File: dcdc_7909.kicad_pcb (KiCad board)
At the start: 4 copper layers, 41.5 x 27 mm, 60 parts, among them J1 V_IN, J2 G_IN, J3 RFShield_Clip, J4 RFShield_Clip, J5 RFShield_Clip, J6 RFShield_Clip, J7 +10V, J8 G_OUT, J9 -10V, U1 LM2940-SOT223-15, U2 LT3471, U3 LT3045xMSE, U4 LT3094xMSE

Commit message: Rev 2.1 finished.
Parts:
- C12: value 470p -> 150p
- C17, C18: value 10u -> 22u; footprint Capacitor_SMD:C_0805_2012Metric -> Capacitor_SMD:C_1206_3216Metric
- C6: value 2200p -> 150p
- R2, R4: value DNP -> 2k
- R3: value 18k -> 20k
- R5: value 2k -> DNP
- R6: value 20k -> 22k
- moved C18 1.46 mm to (85.1, 67.4), turned to 90 degrees
- moved R7 0.58 mm to (87.5, 57.7)
- moved C17 0.56 mm to (87.9, 55.8)
- moved C16 0.53 mm to (81.1, 64.2)
- moved U4 0.53 mm to (85.0, 61.6)
- moved C22 0.53 mm to (89.0, 62.6)
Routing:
- net Net-(C17-Pad1): track 4.46 -> 3.76 mm
- net GND: vias 131 -> 138
- added copper zone on In2.Cu, net /-10.5V

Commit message: Final v2.1.
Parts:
- R2, R4: value 2k -> 2k05

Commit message: V2.1 ready for JLCPCB.
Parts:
- moved R9 1.37 mm to (93.1, 67.4)
- moved R10 0.86 mm to (92.7, 75.5)
- moved R1 0.77 mm to (109.7, 72.2)
- moved C4 0.74 mm to (109.7, 74.7)
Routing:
- net /+10V: track 13.1 -> 14.8 mm
- net Net-(D4-Pad2): track 3.17 -> 4.51 mm
- net Net-(C4-Pad1): track 28.8 -> 27.8 mm
- net Net-(D5-Pad1): track 3.88 -> 4.81 mm
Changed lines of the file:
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@@
   )
   (footprint "Resistor_SMD:R_0603_1608Metric" (layer "F.Cu")
-    (at 92.329 74.676 90)
+    (at 92.71 75.4502 90)
     (descr "Resistor SMD 0603 (1608 Metric), square (rectangular) end terminal, IPC_7351 nominal, (Body size source: IPC-SM-782 page 72, https://www.pcb-3d.com/wordpress/wp-content/uploads/ipc-sm-782a_amendment_1_and_2.pdf), generated with kicad-footprint-generator")
     (tags "resistor")
@@
   )
   (footprint "Resistor_SMD:R_0603_1608Metric" (layer "F.Cu")
-    (at 92.202 68.389 -90)
+    (at 93.1164 67.373 -90)
     (descr "Resistor SMD 0603 (1608 Metric), square (rectangular) end terminal, IPC_7351 nominal, (Body size source: IPC-SM-782 page 72, https://www.pcb-3d.com/wordpress/wp-content/uploads/ipc-sm-782a_amendment_1_and_2.pdf), generated with kicad-footprint-generator")
     (tags "resistor")
@@
     (property "Sheetname" "")
     (attr smd)
-    (fp_text reference "R9" (at -2.222 0 90) (layer "F.SilkS")
+    (fp_text reference "R9" (at -0.063 1.1176 90) (layer "F.SilkS")
       (effects (font (size 1 1) (thickness 0.15)))
     )
@@
     (property "Sheetname" "")
     (attr smd)
-    (fp_text reference "C11" (at 2.7414 0 90) (layer "F.SilkS")
+    (fp_text reference "C11" (at 0.6858 2.0574 180) (layer "F.SilkS")
       (effects (font (size 1 1) (thickness 0.15)))
     )
@@
   )
   (footprint "Capacitor_SMD:C_0603_1608Metric" (layer "F.Cu")
-    (at 110.3884 75.0316 -90)
+    (at 109.728 74.689 -90)
     (descr "Capacitor SMD 0603 (1608 Metric), square (rectangular) end terminal, IPC_7351 nominal, (Body size source: IPC-SM-782 page 76, https://www.pcb-3d.com/wordpress/wp-content/uploads/ipc-sm-782a_amendment_1_and_2.pdf), generated with kicad-footprint-generator")
     (tags "capacitor")
@@
     (property "Sheetname" "")
     (attr smd)
-    (fp_text reference "C4" (at -4.2164 -0.2032 90) (layer "F.SilkS")
+    (fp_text reference "C4" (at 1.8666 0 180) (layer "F.SilkS")
       (effects (font (size 1 1) (thickness 0.15)))
     )
@@
   )
   (footprint "Resistor_SMD:R_0402_1005Metric" (layer "F.Cu")
-    (at 110.3884 72.4916 -90)
+    (at 109.6772 72.1888 -90)
     (descr "Resistor SMD 0402 (1005 Metric), square (rectangular) end terminal, IPC_7351 nominal, (Body size source: IPC-SM-782 page 72, https://www.pcb-3d.com/wordpress/wp-content/uploads/ipc-sm-782a_amendment_1_and_2.pdf), generated with kicad-footprint-generator")
     (tags "resistor")
@@
     (property "Sheetname" "")
     (attr smd)
-    (fp_text reference "R1" (at 4.6482 0 90) (layer "F.SilkS")
+    (fp_text reference "R1" (at 0.0488 -0.9652 90) (layer "F.SilkS")
       (effects (font (size 1 1) (thickness 0.15)))
     )
@@
   )
   (segment (start 101.854 73.1266) (end 101.854 73.41865) (width 1.016) (layer "F.Cu") (net 1))
+  (segment (start 110.4392 71.6788) (end 111.76 70.358) (width 0.25) (layer "F.Cu") (net 1))
   (segment (start 98.171 63.43645) (end 97.24395 62.5094) (width 0.762) (layer "F.Cu") (net 1))
   (segment (start 112.635 73.304) (end 112.635 71.233) (width 0.762) (layer "F.Cu") (net 1))
-  (segment (start 110.3884 71.9816) (end 110.3884 71.7296) (width 0.254) (layer "F.Cu") (net 1))
   (segment (start 104.8004 72.7474) (end 105.078 73.025) (width 1.016) (layer "F.Cu") (net 1))
   (segment (start 98.171 65.786) (end 98.171 63.43645) (width 0.762) (layer "F.Cu") (net 1))
   (segment (start 104.8004 70.5866) (end 104.8004 72.7474) (width 1.016) (layer "F.Cu") (net 1))
-  (segment (start 110.3884 71.7296) (end 111.76 70.358) (width 0.254) (layer "F.Cu") (net 1))
   (segment (start 105.078 73.025) (end 102.24765 73.025) (width 1.016) (layer "F.Cu") (net 1))
   (segment (start 98.9838 66.5988) (end 98.171 65.786) (width 0.762) (layer "F.Cu") (net 1))
   (segment (start 112.635 71.233) (end 111.76 70.358) (width 0.762) (layer "F.Cu") (net 1))
+  (segment (start 109.6772 71.6788) (end 110.4392 71.6788) (width 0.25) (layer "F.Cu") (net 1))
   (segment (start 101.8772 66.6496) (end 99.568 66.6496) (width 0.254) (layer "F.Cu") (net 1))
   (segment (start 99.5172 66.5988) (end 98.9838 66.5988) (width 0.762) (layer "F.Cu") (net 1))
@@
   (segment (start 101.8772 67.1496) (end 100.9984 67.1496) (width 0.1524) (layer "F.Cu") (net 4))
   (segment (start 100.9476 66.1496) (end 100.8211 66.0231) (width 0.1524) (layer "F.Cu") (net 4))
-  (segment (start 110.3884 73.0016) (end 109.5228 73.0016) (width 0.1524) (layer "F.Cu") (net 4))
+  (segment (start 109.6772 72.6988) (end 110.227 72.6988) (width 0.25) (layer "F.Cu") (net 4))
+  (segment (start 109.728 72.7496) (end 109.6772 72.6988) (width 0.25) (layer "F.Cu") (net 4))
   (segment (start 101.8772 66.1496) (end 100.9476 66.1496) (width 0.1524) (layer "F.Cu") (net 4))
-  (segment (start 109.5228 73.0016) (end 109.474 73.0504) (width 0.1524) (layer "F.Cu") (net 4))
+  (segment (start 109.728 73.914) (end 109.728 72.7496) (width 0.25) (layer "F.Cu") (net 4))
   (segment (start 100.9984 67.1496) (end 100.838 67.31) (width 0.1524) (layer "F.Cu") (net 4))
   (segment (start 100.8211 66.0231) (end 100.838 66.0231) (width 0.1524) (layer "F.Cu") (net 4))
-  (segment (start 110.3884 74.2566) (end 110.3884 73.0016) (width 0.1524) (layer "F.Cu") (net 4))
+  (segment (start 110.227 72.6988) (end 110.5916 73.0634) (width 0.25) (layer "F.Cu") (net 4))
   (via (at 100.838 67.31) (size 0.6) (drill 0.3) (layers "F.Cu" "B.Cu") (free) (net 4))
   (via (at 100.838 66.0231) (size 0.6) (drill 0.3) (layers "F.Cu" "B.Cu") (net 4))
-  (via (at 109.474 73.0504) (size 0.6) (drill 0.3) (layers "F.Cu" "B.Cu") (net 4))
-  (segment (start 113.3348 72.136) (end 112.4204 73.0504) (width 0.1524) (layer "In2.Cu") (net 4))
+  (via (at 110.5916 73.0634) (size 0.6) (drill 0.3) (layers "F.Cu" "B.Cu") (net 4))
   (segment (start 100.838 67.31) (end 100.838 66.0231) (width 0.1524) (layer "In2.Cu") (net 4))
   (segment (start 110.6932 64.77) (end 113.3348 67.4116) (width 0.1524) (layer "In2.Cu") (net 4))
+  (segment (start 112.4074 73.0634) (end 110.5916 73.0634) (width 0.1524) (layer "In2.Cu") (net 4))
   (segment (start 113.3348 67.4116) (end 113.3348 72.136) (width 0.1524) (layer "In2.Cu") (net 4))
+  (segment (start 113.3348 72.136) (end 112.4074 73.0634) (width 0.1524) (layer "In2.Cu") (net 4))
   (segment (start 100.838 66.0231) (end 102.0911 64.77) (width 0.1524) (layer "In2.Cu") (net 4))
-  (segment (start 112.4204 73.0504) (end 109.474 73.0504) (width 0.1524) (layer "In2.Cu") (net 4))
   (segment (start 102.0911 64.77) (end 110.6932 64.77) (width 0.1524) (layer "In2.Cu") (net 4))
   (segment (start 107.3216 69.4824) (end 107.2896 69.5144) (width 0.254) (layer "F.Cu") (net 7))
@@
   (segment (start 104.9108 67.7832) (end 107.2896 67.7832) (width 0.1524) (layer "F.Cu") (net 10))
   (segment (start 89.027 66.837) (end 89.2 67.01) (width 0.508) (layer "F.Cu") (net 11))
-  (segment (start 92.202 67.564) (end 89.754 67.564) (width 0.3048) (layer "F.Cu") (net 11))
+  (segment (start 92.6544 67.01) (end 89.2 67.01) (width 0.25) (layer "F.Cu") (net 11))
   (segment (start 89.027 64.0552) (end 89.027 66.837) (width 0.508) (layer "F.Cu") (net 11))
+  (segment (start 93.1164 66.548) (end 92.6544 67.01) (width 0.25) (layer "F.Cu") (net 11))
   (via (at 81.9912 68.1228) (size 0.8) (drill 0.4) (layers "F.Cu" "B.Cu") (net 11))
   (segment (start 89.2 67.01) (end 83.104 67.01) (width 1.016) (layer "B.Cu") (net 11))
@@
   (segment (start 81.8642 55.753) (end 83.009 55.753) (width 1.016) (layer "F.Cu") (net 12))
   (segment (start 83.009 55.753) (end 83.136 55.626) (width 1.016) (layer "F.Cu") (net 12))
-  (segment (start 92.329 75.501) (end 90.709 75.501) (width 0.3048) (layer "F.Cu") (net 12))
   (segment (start 86.819 79.248) (end 86.962 79.248) (width 0.762) (layer "F.Cu") (net 12))
   (segment (start 86.962 79.248) (end 89.2 77.01) (width 0.762) (layer "F.Cu") (net 12))
-  (segment (start 90.709 75.501) (end 89.2 77.01) (width 0.3048) (layer "F.Cu") (net 12))
+  (segment (start 91.9752 77.01) (end 89.2 77.01) (width 0.25) (layer "F.Cu") (net 12))
+  (segment (start 92.71 76.2752) (end 91.9752 77.01) (width 0.25) (layer "F.Cu") (net 12))
   (via (at 81.8642 55.753) (size 0.8) (drill 0.4) (layers "F.Cu" "B.Cu") (net 12))
   (segment (start 82.6996 77.01) (end 80.6196 74.93) (width 1.016) (layer "In2.Cu") (net 12))
@@
   (segment (start 80.6196 74.93) (end 80.6196 63.5508) (width 1.016) (layer "In2.Cu") (net 12))
   (segment (start 81.1784 56.4388) (end 81.8642 55.753) (width 1.016) (layer "In2.Cu") (net 12))
-  (segment (start 92.202 69.214) (end 91.9744 69.214) (width 0.254) (layer "F.Cu") (net 13))
-  (segment (start 91.9744 69.214) (end 91.2876 69.9008) (width 0.254) (layer "F.Cu") (net 13))
+  (segment (start 93.1164 68.198) (end 92.9904 68.198) (width 0.25) (layer "F.Cu") (net 13))
+  (segment (start 92.9904 68.198) (end 91.2876 69.9008) (width 0.25) (layer "F.Cu") (net 13))
   (via (at 91.2876 69.9008) (size 0.6) (drill 0.3) (layers "F.Cu" "B.Cu") (net 13))
   (segment (start 92.819 68.834) (end 92.3544 68.834) (width 0.254) (layer "B.Cu") (net 13))
   (segment (start 92.3544 68.834) (end 91.2876 69.9008) (width 0.254) (layer "B.Cu") (net 13))
-  (segment (start 91.5924 73.1144) (end 92.329 73.851) (width 0.254) (layer "F.Cu") (net 14))
-  (segment (start 91.5924 72.009) (end 91.5924 73.1144) (width 0.254) (layer "F.Cu") (net 14))
+  (segment (start 91.5924 73.5076) (end 92.71 74.6252) (width 0.25) (layer "F.Cu") (net 14))
+  (segment (start 91.5924 72.009) (end 91.5924 73.5076) (width 0.25) (layer "F.Cu") (net 14))
   (via (at 91.5924 72.009) (size 0.6) (drill 0.3) (layers "F.Cu" "B.Cu") (net 14))
   (segment (start 91.5924 71.9656) (end 92.819 70.739) (width 0.254) (layer "B.Cu") (net 14))

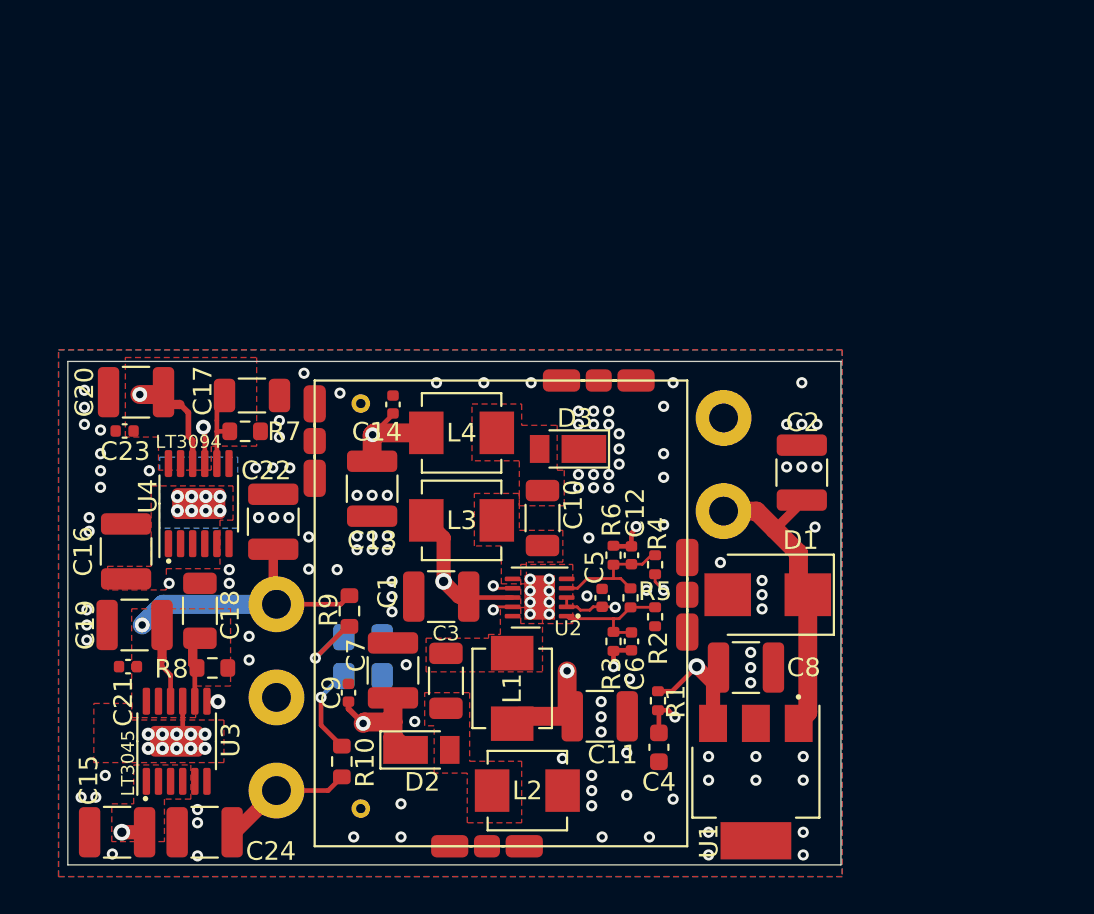
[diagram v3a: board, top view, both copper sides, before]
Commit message: Reworking the board with MAX76x/
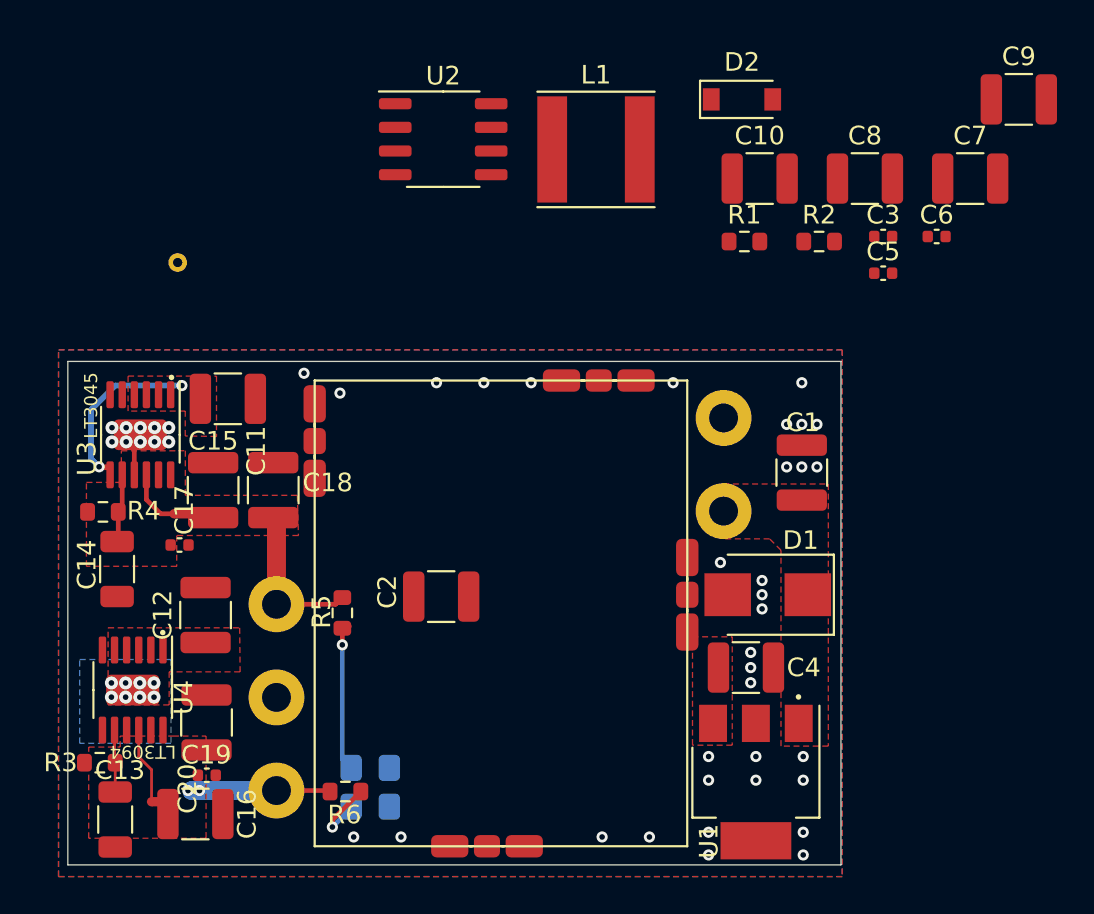
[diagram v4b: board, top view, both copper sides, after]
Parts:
- removed the C11 at (106.6, 73.0)
- removed the C12 at (108.3, 64.4)
- removed the C13 at (94.3, 60.8)
- removed the C14 at (95.5, 56.3)
- removed the C4 at (109.7, 74.7)
- removed the D3 at (104.9, 58.7)
- removed L2, L3, L4: 10u, Inductor_SMD:L_Vishay_IHLP-1616
- removed the R3 at (107.3, 69.0)
- removed the R4 at (109.5, 64.9)
- removed the R5 at (108.2, 66.7)
- removed the R6 at (107.3, 64.4)
- removed the TP1 at (93.7, 78.0)
- added C8: 22u, Capacitor_SMD:C_1210_3225Metric, F.Cu at (120.8, 44.2)
- C10: value 4u7 -> 22u; footprint Capacitor_SMD:C_1206_3216Metric -> Capacitor_SMD:C_1210_3225Metric
- C3: value 4u7 -> 100n; footprint Capacitor_SMD:C_1206_3216Metric -> Capacitor_SMD:C_0402_1005Metric
- C6: value 150p -> 100n
- C9: value 10n -> 22u; footprint Capacitor_SMD:C_0402_1005Metric -> Capacitor_SMD:C_1210_3225Metric
- D2: value D_Schottky -> 1N5817; footprint Diode_SMD:D_PowerDI-123 -> Diode_SMD:D_SOD-123
- L1: value 10u -> 47u; footprint Inductor_SMD:L_Vishay_IHLP-1616 -> Inductor_SMD:L_Taiyo-Yuden_NR-60xx
- R1: value 20k -> 1M07 1%; footprint Resistor_SMD:R_0402_1005Metric -> Resistor_SMD:R_0603_1608Metric
- R2: value 2k05 -> 150k 1%; footprint Resistor_SMD:R_0402_1005Metric -> Resistor_SMD:R_0603_1608Metric
- TP1: renamed from TP2; value -10.5V -> -10.7
- U2: value LT3471 -> MAX764; footprint Package_DFN_QFN:DFN-10-1EP_3x3mm_P0.5mm_EP1.65x2.38mm -> Package_SO:SO-8_3.9x4.9mm_P1.27mm
- moved C9 48.1 mm to (129.0, 39.9), turned to 0 degrees
- moved C7 40.7 mm to (126.4, 44.2), turned to 0 degrees
- moved D2 38.9 mm to (114.2, 39.9)
- moved C3 33.5 mm to (121.8, 47.3), turned to 0 degrees
- moved L1 29.3 mm to (106.3, 42.6), turned to 0 degrees
- moved C6 27.2 mm to (124.6, 47.3), turned to 0 degrees
- moved U2 25.1 mm to (98.1, 42.0), turned to 0 degrees
- moved R1 25.1 mm to (114.3, 47.5), turned to 0 degrees
- moved C11 24.0 mm to (86.6, 56.0), turned to 0 degrees
- moved C13 23.9 mm to (80.5, 78.6), turned to -90 degrees
- moved C5 23.1 mm to (121.8, 49.2), turned to 0 degrees
- moved C16 22.9 mm to (84.8, 78.3), turned to 0 degrees
- moved R2 22.0 mm to (118.3, 47.5), turned to 0 degrees
- moved C10 21.6 mm to (115.1, 44.2), turned to 0 degrees
- moved NT2 21.3 mm to (83.0, 77.6), turned to 0 degrees
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- renumbered C2 to C1, C15 to C11, C16 to C12, C17 to C13, C18 to C14, C19 to C15, C20 to C16, C21 to C17, C22 to C18, C23 to C19, C1 to C2, C24 to C20, C8 to C4, D4 to D3, D5 to D4, R7 to R3, R8 to R4, R9 to R5, R10 to R6
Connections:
- C10 pad 1: Net-(C10-Pad1) -> VCC
- C10 pad 2: Net-(C10-Pad2) -> GND
- C11 pad 1: /+10.5V -> VCC
- C12 pad 1: /-10.5V -> /-10.7
- C3 pad 1: Net-(C3-Pad1) -> VCC
- C3 pad 2: Net-(C3-Pad2) -> GND
- C6 pad 1: /+10.5V -> /-10.7
- C6 pad 2: Net-(C6-Pad2) -> GND
- C7 pad 1: /+10.5V -> /-10.7
- C9 pad 1: /+10.5V -> /-10.7
- D2 pad 1: /+10.5V -> Net-(D2-Pad1)
- D2 pad 2: Net-(C3-Pad2) -> /-10.7
- L1 pad 1: VCC -> Net-(D2-Pad1)
- L1 pad 2: Net-(C3-Pad1) -> GND
- R1 pad 1: VCC -> Net-(R1-Pad1)
- R1 pad 2: Net-(C4-Pad1) -> /-10.7
- R2 pad 1: GND -> Net-(C5-Pad1)
- R2 pad 2: Net-(C6-Pad2) -> Net-(R1-Pad1)
- TP1 pad 1: /-10.5V -> /-10.7
- U2 pad 1: Net-(C6-Pad2) -> /-10.7
- U2 pad 2: Net-(C5-Pad1) -> Net-(R1-Pad1)
- U2 pad 3: Net-(C5-Pad1) -> GND
- U2 pad 4: Net-(C12-Pad2) -> Net-(C5-Pad1)
- U2 pad 6: Net-(C10-Pad1) -> VCC
- U2 pad 7: Net-(C4-Pad1) -> VCC
- U2 pad 8: VCC -> Net-(D2-Pad1)
- U3 pad 1: /+10.5V -> VCC
- U3 pad 2: /+10.5V -> VCC
- U3 pad 3: /+10.5V -> VCC
- U3 pad 4: /+10.5V -> VCC
- U3 pad 7: /+10.5V -> VCC
- U4 pad 1: /-10.5V -> /-10.7
- U4 pad 13: /-10.5V -> /-10.7
- U4 pad 2: /-10.5V -> /-10.7
- U4 pad 3: /-10.5V -> /-10.7
- U4 pad 5: /-10.5V -> /-10.7
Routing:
- net /+10.5V: track 62.9 -> 0.00 mm, vias 4 -> 0
- net /-10.5V: track 40.7 -> 0.00 mm, vias 10 -> 0
- net /-10V: track 37.6 -> 7.32 mm, vias 1 -> 2
- net VCC: track 38.2 -> 9.37 mm, vias 3 -> 2
- net Net-(C4-Pad1): track 27.8 -> 0.00 mm, vias 3 -> 0
- net Net-(C1-Pad1): track 16.0 -> 0.00 mm
- net Net-(C5-Pad1): track 7.60 -> 0.00 mm, vias 2 -> 0
- net Net-(C12-Pad2): track 6.85 -> 0.00 mm
- net Net-(C6-Pad2): track 6.54 -> 0.00 mm
- net /+10V: track 14.8 -> 8.41 mm, vias 1 -> 0
- net Net-(D3-Pad2): track 4.51 -> 7.82 mm
- net GND: track 3.76 -> 2.28 mm, vias 138 -> 44
- net Net-(NT2-Pad1): track 2.92 -> 4.13 mm
- net Net-(D4-Pad1): track 4.81 -> 4.05 mm
- net Net-(NT1-Pad1): track 2.46 -> 3.13 mm
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- added copper zone on B.Cu, net /-10.7
- added copper zone on F.Cu, net /-10.7
- added copper zone on F.Cu, net Net-(C1-Pad1)
- added copper zone on F.Cu, net VCC
- removed copper zone on F.Cu, net /+10.5V
- removed copper zone on B.Cu, net /-10.5V
- removed copper zone on F.Cu, net /-10.5V
- removed copper zone on In2.Cu, net /-10.5V
- removed copper zone on F.Cu, net Net-(C10-Pad1)
- removed copper zone on F.Cu, net Net-(C10-Pad2)
- removed copper zone on F.Cu, net Net-(C3-Pad1)
- removed copper zone on F.Cu, net Net-(C3-Pad2)
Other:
- board text removed: "+"
- board text removed: "+10V"
- board text removed: "-10V"

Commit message: Reworking almost completed.
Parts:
- added C1: 22u, Capacitor_SMD:C_1210_3225Metric, F.Cu at (108.8, 71.2)
- D2: footprint Diode_SMD:D_SOD-123 -> Diode_SMD:D_PowerDI-123
- J3, J4, J5, J6: value RFShield_Clip -> Conn_01x01; footprint marcin_library:S0971-46R -> Connector_Wire:SolderWirePad_1x01_SMD_1x2mm
- R1, R2, R5, R6: footprint Resistor_SMD:R_0603_1608Metric -> Resistor_SMD:R_0402_1005Metric
- moved C10 44.7 mm to (93.7, 67.3), turned to 90 degrees
- moved C9 38.9 mm to (93.7, 72.0), turned to -90 degrees
- moved C7 37.7 mm to (96.8, 72.8), turned to -90 degrees
- moved C8 36.4 mm to (98.0, 66.9)
- moved C6 36.3 mm to (98.1, 76.8), turned to -90 degrees
- moved D2 34.1 mm to (97.9, 69.8), turned to 180 degrees
- moved R2 33.4 mm to (98.1, 74.2), turned to 90 degrees
- moved R1 32.2 mm to (96.6, 74.4), turned to 180 degrees
- moved U2 32.2 mm to (102.5, 73.9)
- moved C4 31.9 mm to (106.7, 75.4), turned to -90 degrees
- moved C11 26.6 mm to (92.3, 57.7), turned to -90 degrees
- moved J6 25.7 mm to (102.0, 80.3), turned to 90 degrees
- moved L1 25.1 mm to (103.6, 67.5), turned to 90 degrees
- moved TP1 20.1 mm to (96.5, 64.3)
- moved J4 17.1 mm to (111.3, 66.7)
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- renumbered C9 to C10, C10 to C11, C11 to C12, C12 to C13, C13 to C14, C14 to C15, C15 to C16, C16 to C17, C17 to C18, C18 to C19, C1 to C2, C19 to C20, C20 to C21, C2 to C3, C3 to C4, C4 to C5, C5 to C6, C6 to C7, C7 to C8, C8 to C9
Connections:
- net Net-(R1-Pad1) renamed /FB
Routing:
- net VCC: track 9.37 -> 50.5 mm, vias 2 -> 13
- net /-10.7: track 0.00 -> 9.86 mm, vias 8 -> 10
- net Net-(D2-Pad1): track 0.00 -> 7.65 mm
- net Net-(D3-Pad2): track 7.82 -> 14.6 mm
- net Net-(C6-Pad1): track 0.00 -> 3.31 mm
- net /FB: track 0.00 -> 3.23 mm
- net Net-(D4-Pad1): track 4.05 -> 2.32 mm
- net GND: vias 44 -> 54
